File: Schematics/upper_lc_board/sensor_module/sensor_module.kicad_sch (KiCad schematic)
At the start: 49 parts, among them J2 HALL, J3 PT1, J4 PT2, J7 TC, U10 OA-TLV9001IDCK, U11 OA-TLV9001IDCK, U12 OA-TLV9001IDCK, U7 ADC_ADS131M04IPWR

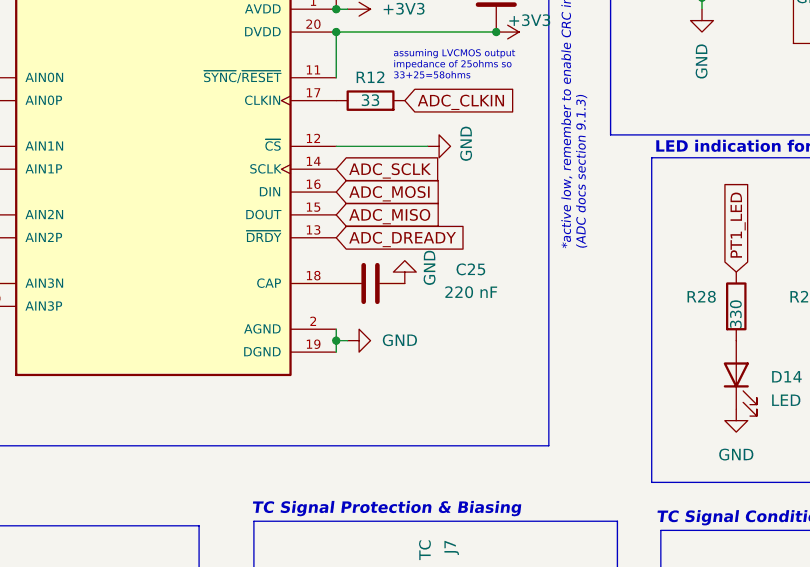
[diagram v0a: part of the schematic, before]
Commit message: switching to primarily 0603 footprints and started adding LSCS numbers
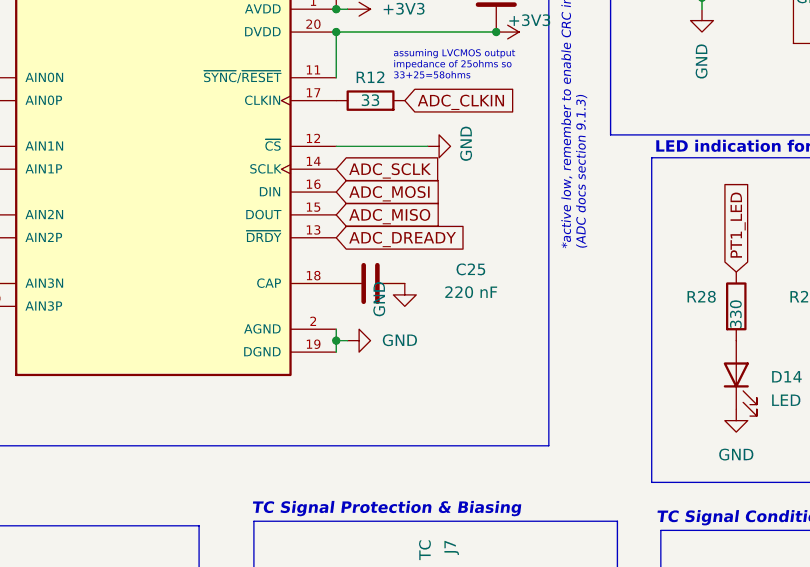
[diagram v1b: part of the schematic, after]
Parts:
- C17, C26, C30, C31, C4, C9: LCSC (none) -> C14663
- C18, C19, C20: LCSC (none) -> C96446
- C22, C23: LCSC (none) -> C15849
- C25: footprint Capacitor_SMD:C_0402_1005Metric -> Resistor_SMD:R_0603_1608Metric; LCSC (none) -> C16772
- R12: LCSC (none) -> C23140
- R16, R17: footprint Resistor_SMD:R_0402_1005Metric -> Resistor_SMD:R_0603_1608Metric; LCSC (none) -> C4190
- R18, R19: footprint Resistor_SMD:R_0402_1005Metric -> Resistor_SMD:R_0603_1608Metric; LCSC (none) -> C22888
- R28, R29, R30, R31: footprint Resistor_SMD:R_0402_1005Metric -> Resistor_SMD:R_0603_1608Metric; LCSC (none) -> C23138
- R32, R33, R34, R35, R36: footprint Resistor_SMD:R_0402_1005Metric -> Resistor_SMD:R_0603_1608Metric; LCSC (none) -> C21190
- R37: footprint Resistor_SMD:R_0402_1005Metric -> Resistor_SMD:R_0603_1608Metric; Field5 (none) -> C21190
- R44, R45, R5: footprint Resistor_SMD:R_0402_1005Metric -> Resistor_SMD:R_0603_1608Metric; LCSC (none) -> C25804
- R46, R47: LCSC (none) -> C22935
- TH1: footprint Resistor_SMD:R_0402_1005Metric -> Resistor_SMD:R_0603_1608Metric_Pad0.98x0.95mm_HandSolder; Digikey (none) -> 273-TX06F103F3435ERCT-ND; Model (none) -> TX06F103F3435ER

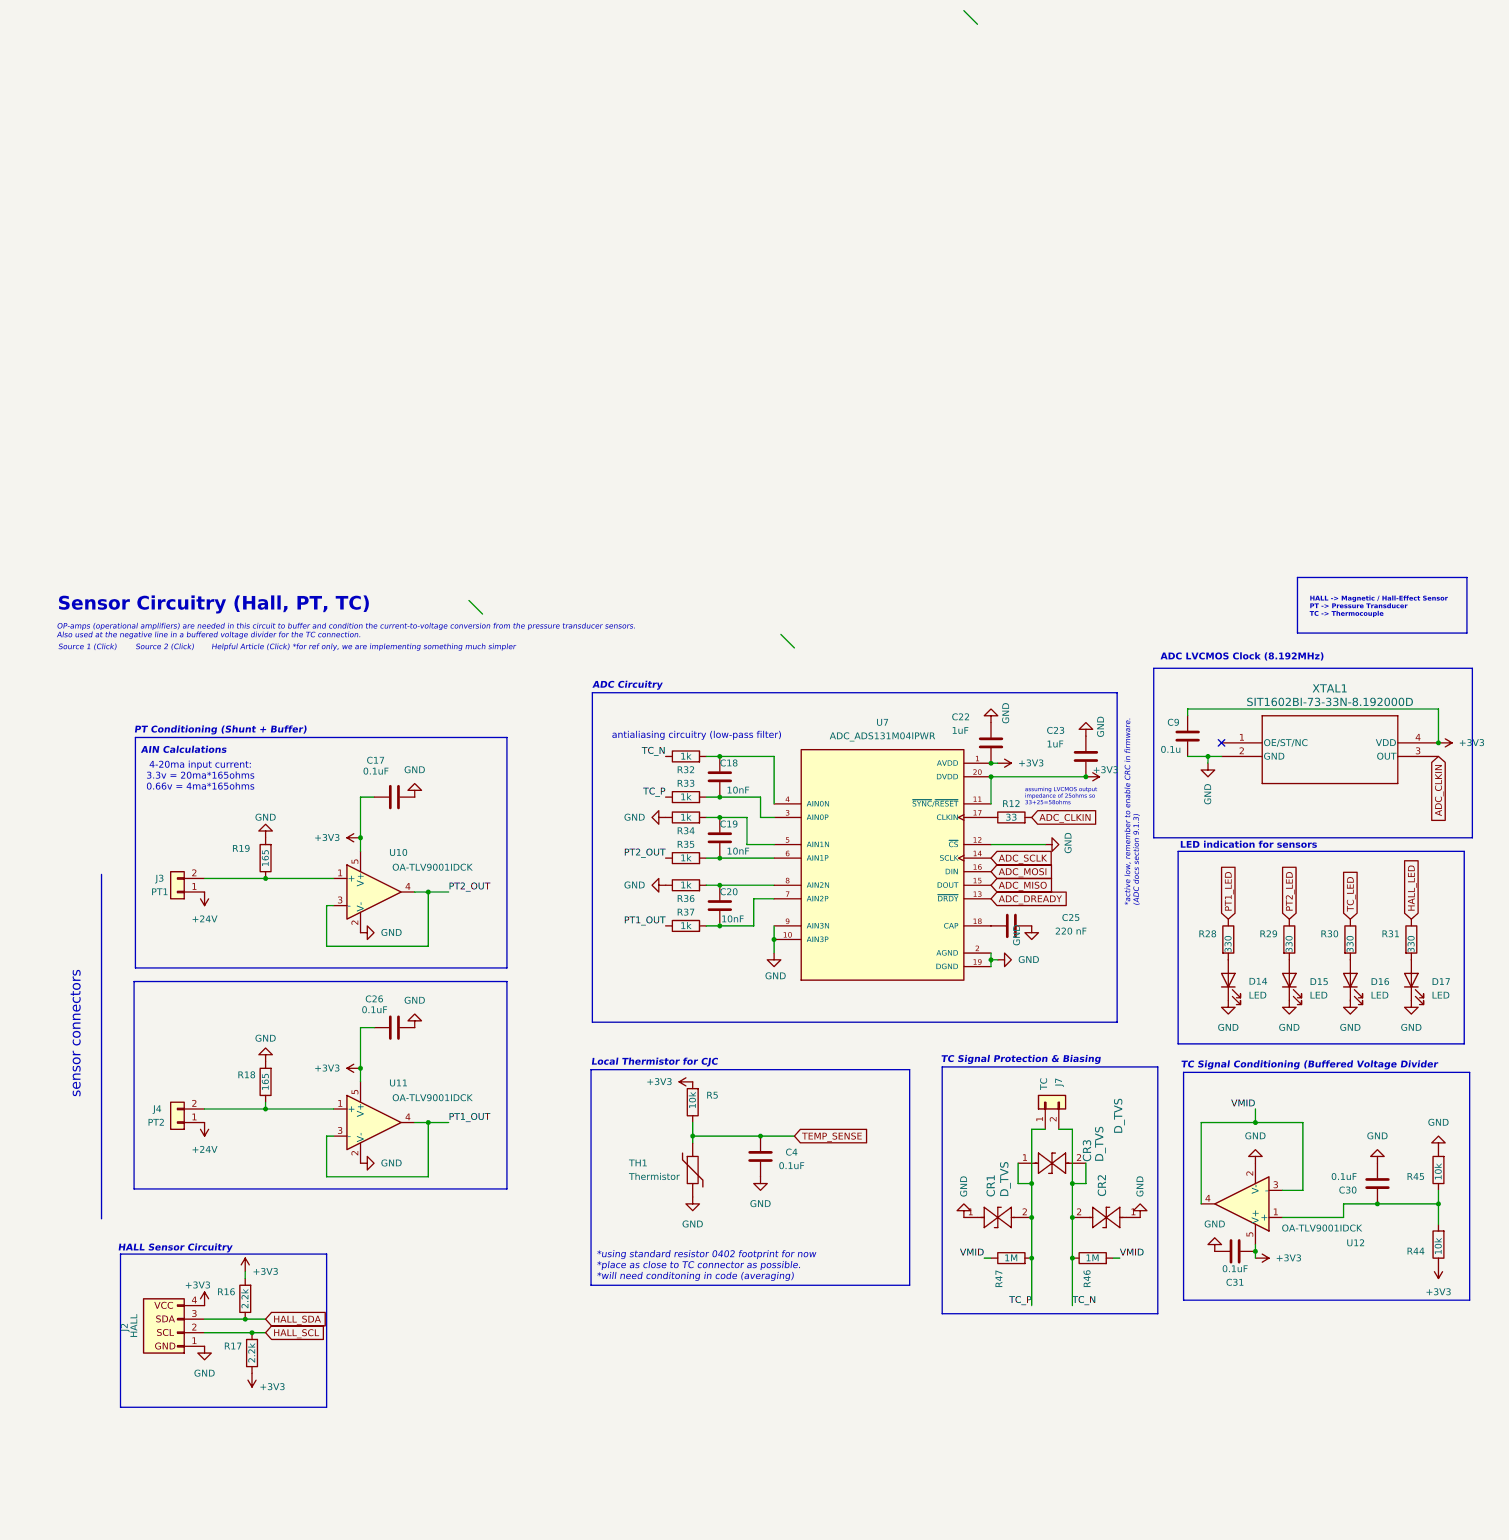
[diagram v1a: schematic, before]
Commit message: added most part number (LCSC, Digikey), verified current limiting resitors
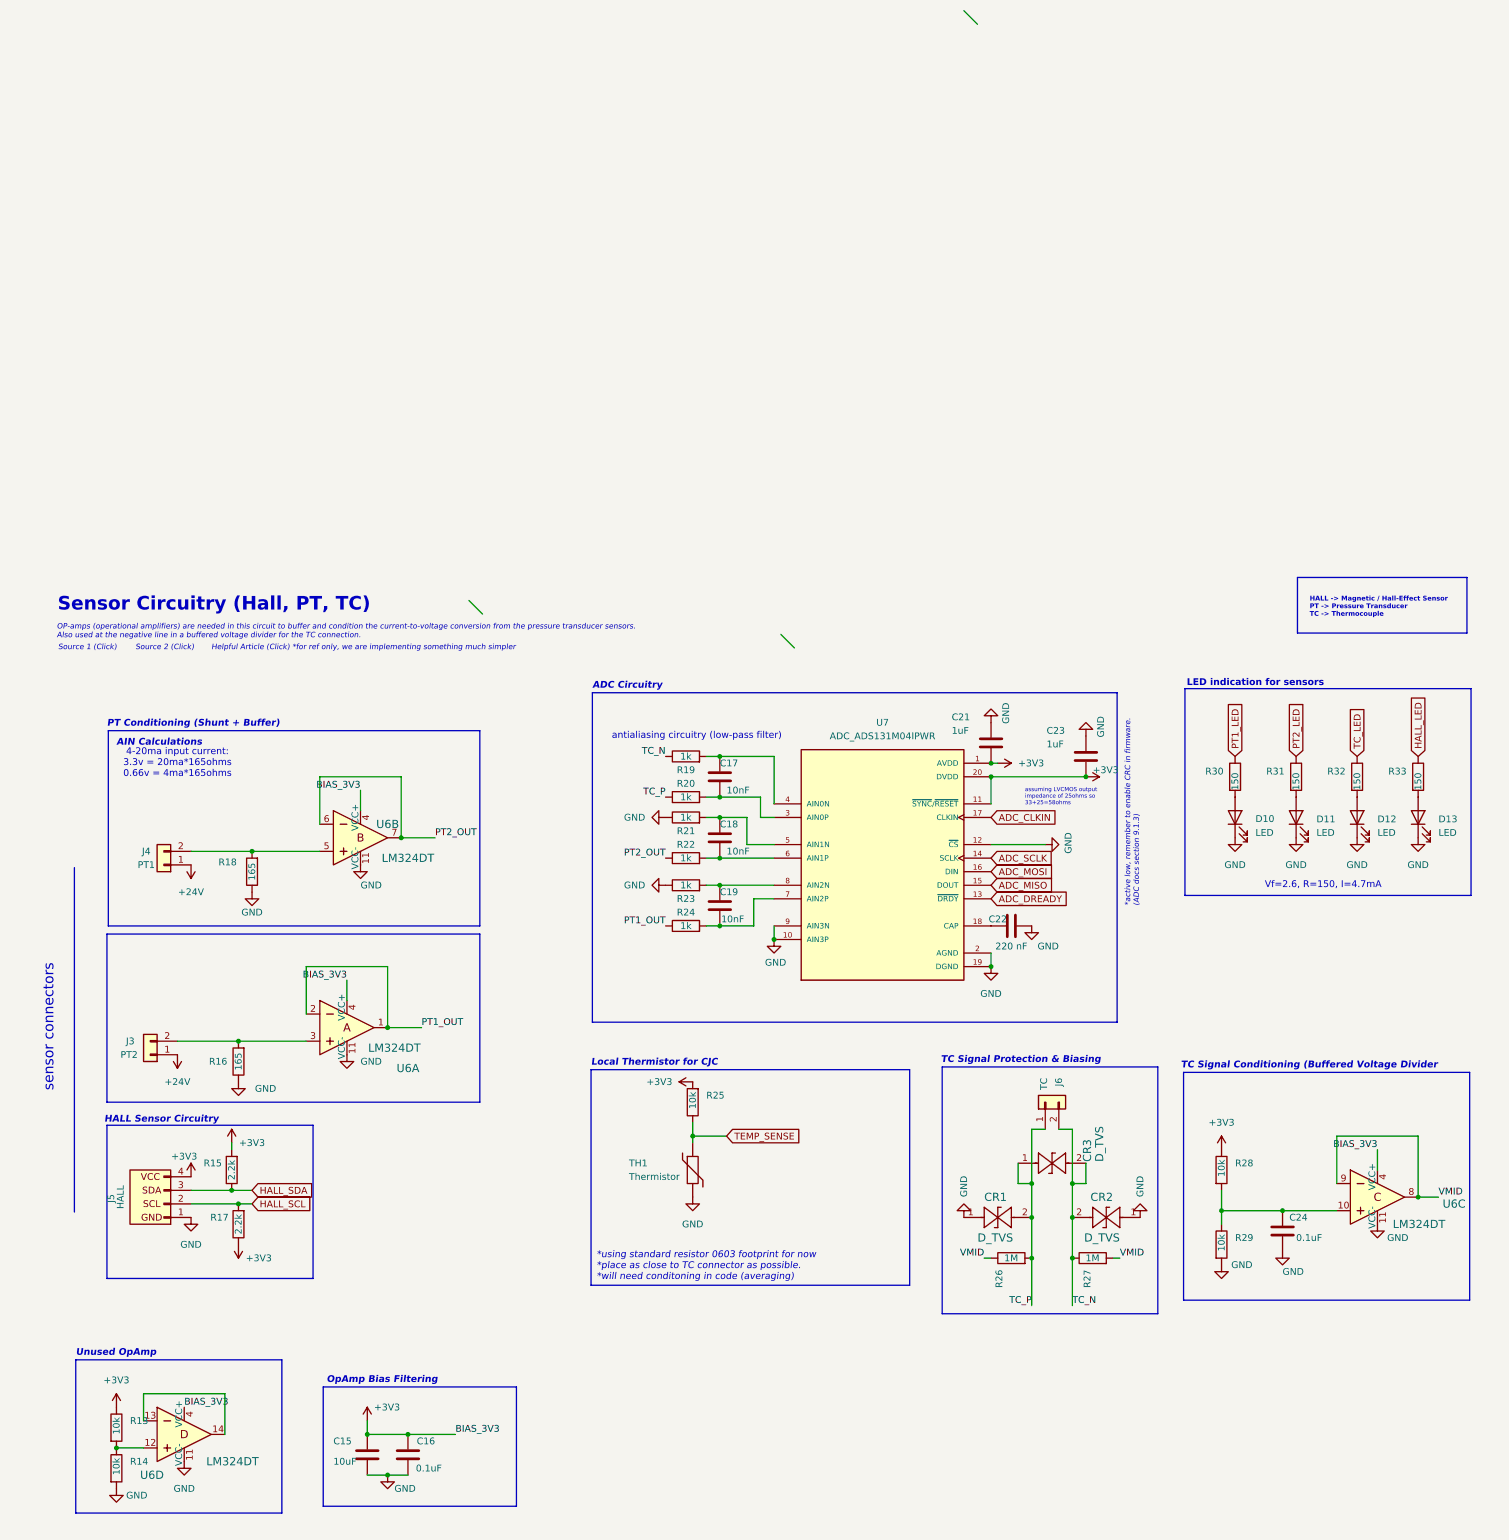
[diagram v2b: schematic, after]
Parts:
- removed C17, C26, C30, C31, C4: 0.1uF, Capacitor_SMD:C_0603_1608Metric, symbol Device:C
- removed C9: 0.1u, Capacitor_SMD:C_0603_1608Metric, symbol Device:C
- removed R12: 33, Resistor_SMD:R_0402_1005Metric, symbol Device:R
- removed R19: 165, Resistor_SMD:R_0603_1608Metric, symbol Device:R
- removed U10, U11, U12: OA-TLV9001IDCK, Package_TO_SOT_SMD:SOT-353_SC-70-5, symbol Amplifier_Operational:TLV9001IDCK
- removed XTAL1: SIT1602BI-73-33N-8.192000D, SON4_SIT1602-7_SIT, symbol SIT1602BI-73-33N-8-19200:SIT1602BI-73-33E-10.000000D
- added C15: 10uF, Capacitor_SMD:C_0603_1608Metric, symbol Device:C
- added C16, C24: 0.1uF, Capacitor_SMD:C_0603_1608Metric, symbol Device:C
- added R13, R14: 10k, Resistor_SMD:R_0603_1608Metric, symbol Device:R
- added R16: 165, Resistor_SMD:R_0805_2012Metric_Pad1.20x1.40mm_HandSolder, symbol Device:R
- added U6: LM324DT, digikey-footprints:SOIC-14_W3.9mm, symbol dk_Linear-Amplifiers-Instrumentation-OP-Amps-Buffer-Amps:LM324DT
- C17: renamed from C18; LCSC C96446 -> C1589
- C18: renamed from C19; LCSC C96446 -> C1589
- C19: renamed from C20; LCSC C96446 -> C1589
- D10: renamed from D14; footprint LED_SMD:LED_0805_2012Metric -> LED_SMD:LED_0603_1608Metric; LCSC (none) -> C2290
- D11: renamed from D15; footprint LED_SMD:LED_0805_2012Metric -> LED_SMD:LED_0603_1608Metric; LCSC (none) -> C2290
- D12: renamed from D16; footprint LED_SMD:LED_0805_2012Metric -> LED_SMD:LED_0603_1608Metric; LCSC (none) -> C2290
- D13: renamed from D17; footprint LED_SMD:LED_0805_2012Metric -> LED_SMD:LED_0603_1608Metric; LCSC (none) -> C2290
- J3: renamed from J4; Digikey (none) -> 900-0530470260-ND
- J4: renamed from J3; Digikey (none) -> 900-0530470260-ND
- J5: renamed from J2; Digikey (none) -> 900-0530470460-ND
- J6: renamed from J7; Digikey (none) -> 900-0530470260-ND
- R18: footprint Resistor_SMD:R_0603_1608Metric -> Resistor_SMD:R_0805_2012Metric_Pad1.20x1.40mm_HandSolder; Digikey (none) -> 311-165CRCT-ND; LCSC C22888 -> (none)
- R30: renamed from R28; value 330 -> 150; LCSC C23138 -> C22808
- R31: renamed from R29; value 330 -> 150; LCSC C23138 -> C22808
- R32: renamed from R30; value 330 -> 150; LCSC C23138 -> C22808
- R33: renamed from R31; value 330 -> 150; LCSC C23138 -> C22808
- U7: LCSC (none) -> C2862562
- renumbered C22 to C21, C25 to C22, R16 to R15, R32 to R19, R33 to R20, R34 to R21, R35 to R22, R36 to R23, R37 to R24, R5 to R25, R47 to R26, R46 to R27, R44 to R28, R45 to R29
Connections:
- net +3V3: now also C15.1, C16.2, R13.1, U6.4 (VCC+), U6.4 (VCC+), U6.4 (VCC+), U6.4 (VCC+)
- net ADC_CLKIN: now also U7.17 (CLKIN)
- net GND: now also R18.1, C15.2, C16.1, C24.2, R14.2, R16.1, U6.11 (VCC-), U6.11 (VCC-), U6.11 (VCC-), U6.11 (VCC-); no longer R18.2
- net PT1_OUT: now also U6.1, U6.2
- net PT2_OUT: now also U6.6, U6.7
- net VMID: now also U6.8, U6.9
- net at R28.2, R29.1: now also C24.1, U6.10
- net at J3.2 (Pin_2): now also R16.2, U6.3; no longer R18.1
- net at J4.2 (Pin_2): now also R18.2, U6.5
- new net: R13.2, R14.1, U6.12
- new net: U6.13, U6.14
- no-connect marks 1 -> 0
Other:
- note added: "*using standard resistor 0603 footprint for now *place as close to TC connector as possible. *will need conditoning in code (averaging)"
- note added: "OpAmp Bias Filtering"
- note added: "Unused OpAmp"
- note added: "Vf=2.6, R=150, I=4.7mA"
- note removed: "*using standard resistor 0402 footprint for now *place as close to TC connector as possible. *will need conditoning in code (averaging)"
- note removed: "ADC LVCMOS Clock (8.192MHz)"
- moved on the sheet: D10, D11, D12, D13, J3, J4, J5, R15, R17, R28, R29, R30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

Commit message: final pcb routing and part numbers
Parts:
- removed R13, R14: 10k, Resistor_SMD:R_0603_1608Metric, symbol Device:R
- renumbered J6 to J7
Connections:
- net V_DIVIDER: now reaches C24.1, R28.2, R29.1, U6.10
- net V_DIVIDER: now also U6.12

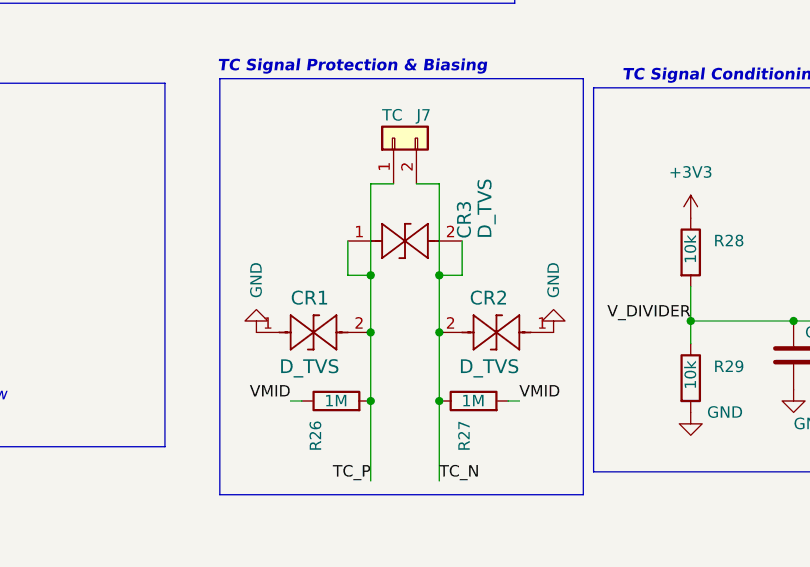
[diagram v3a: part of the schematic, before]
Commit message: fix failed merge, fix part number issues
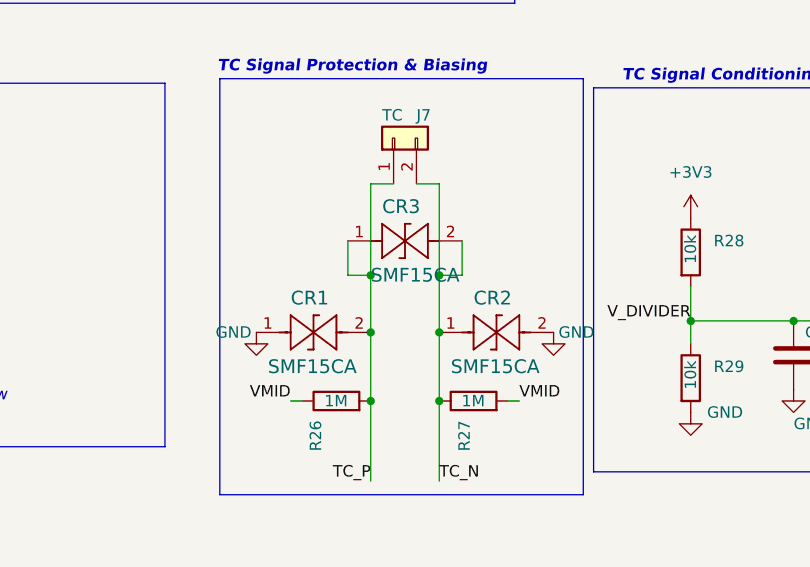
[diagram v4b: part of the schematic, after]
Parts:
- CR1, CR2, CR3: value D_TVS -> SMF15CA
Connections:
- net GND: now also CR2.2; no longer CR2.1
- net TC_N: now also CR2.1; no longer CR2.2

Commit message: cleanup thermocouple routing, add ground pour for thermistor
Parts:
- R24: Field5 C21190 -> (none); LCSC (none) -> C21190
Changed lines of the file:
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@@
 			)
 		)
-		(property "Field5" "C21190"
+		(property "LCSC" "C21190"
 			(at 134.62 80.01 90)
 			(effects

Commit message: clean up silkscreen and routing
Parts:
- CR1, CR2, CR3: LCSC (none) -> C123803
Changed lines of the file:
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@@
 			)
 		)
+		(property "LCSC" "C123803"
+			(at 219.71 134.62 0)
+			(effects
+				(font
+					(size 1.27 1.27)
+				)
+				(hide yes)
+			)
+		)
 		(pin "1"
 		)
@@
 			)
 		)
+		(property "LCSC" "C123803"
+			(at 199.39 134.62 0)
+			(effects
+				(font
+					(size 1.27 1.27)
+				)
+				(hide yes)
+			)
+		)
 		(pin "1"
 		)
@@
 			(at 209.55 124.46 0)
 			(effects
+				(font
+					(size 1.27 1.27)
+				)
+				(hide yes)
+			)
+		)
+		(property "LCSC" "C123803"
+			(at 209.55 124.46 0)
+			(effects

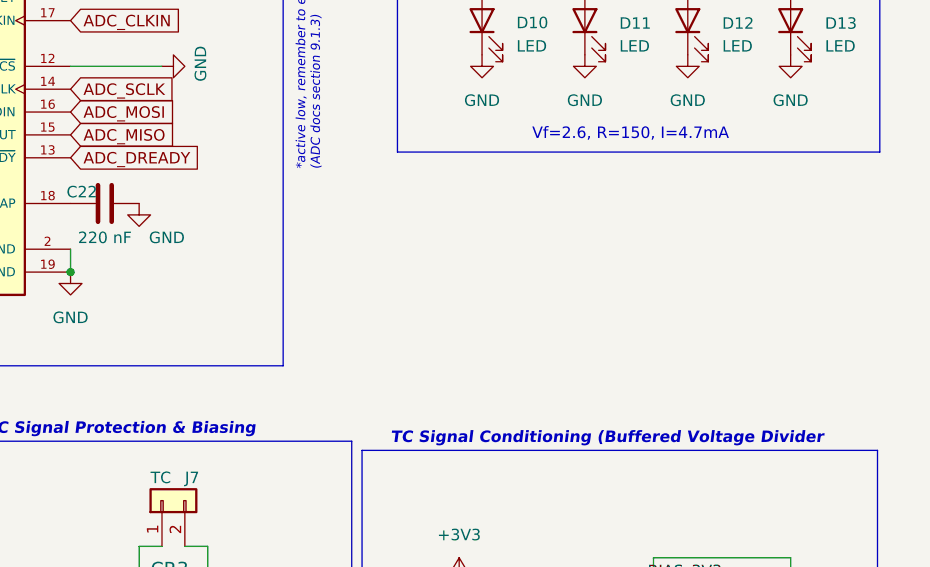
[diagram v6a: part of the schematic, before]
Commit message: fixed incorrect footprints and part numbers
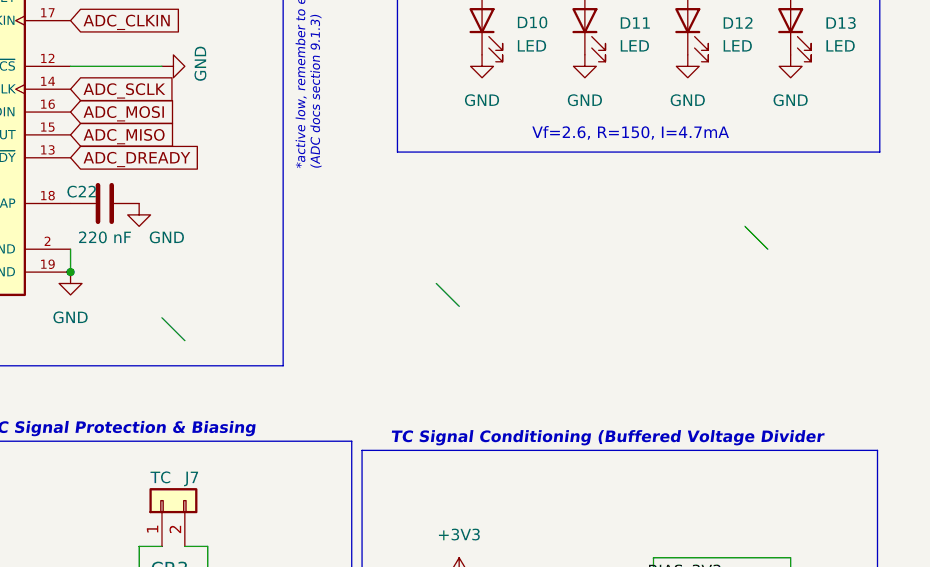
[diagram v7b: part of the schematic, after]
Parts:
- C22: footprint Resistor_SMD:R_0603_1608Metric -> Capacitor_SMD:C_0805_2012Metric; LCSC C16772 -> C5378
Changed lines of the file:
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@@
 	)
 	(bus_entry
+		(at 201.93 92.71)
+		(size 2.54 2.54)
+		(stroke
+			(width 0)
+			(type default)
+		)
+	)
+	(bus_entry
 		(at 93.98 19.05)
 		(size 2.54 2.54)
@@
 	)
 	(bus_entry
+		(at 266.7 82.55)
+		(size 2.54 2.54)
+		(stroke
+			(width 0)
+			(type default)
+		)
+	)
+	(bus_entry
+		(at 232.41 88.9)
+		(size 2.54 2.54)
+		(stroke
+			(width 0)
+			(type default)
+		)
+	)
+	(bus_entry
 		(at 186.69 -91.44)
 		(size 2.54 2.54)
@@
 			)
 		)
-		(property "Footprint" "Resistor_SMD:R_0603_1608Metric"
+		(property "Footprint" "Capacitor_SMD:C_0805_2012Metric"
 			(at 199.39 79.0448 0)
 			(effects
@@
 			)
 		)
-		(property "LCSC" "C16772"
+		(property "LCSC" "C5378"
 			(at 195.58 80.01 90)
 			(effects
